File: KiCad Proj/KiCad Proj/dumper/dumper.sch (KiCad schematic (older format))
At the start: 2 parts, among them J2 SPI

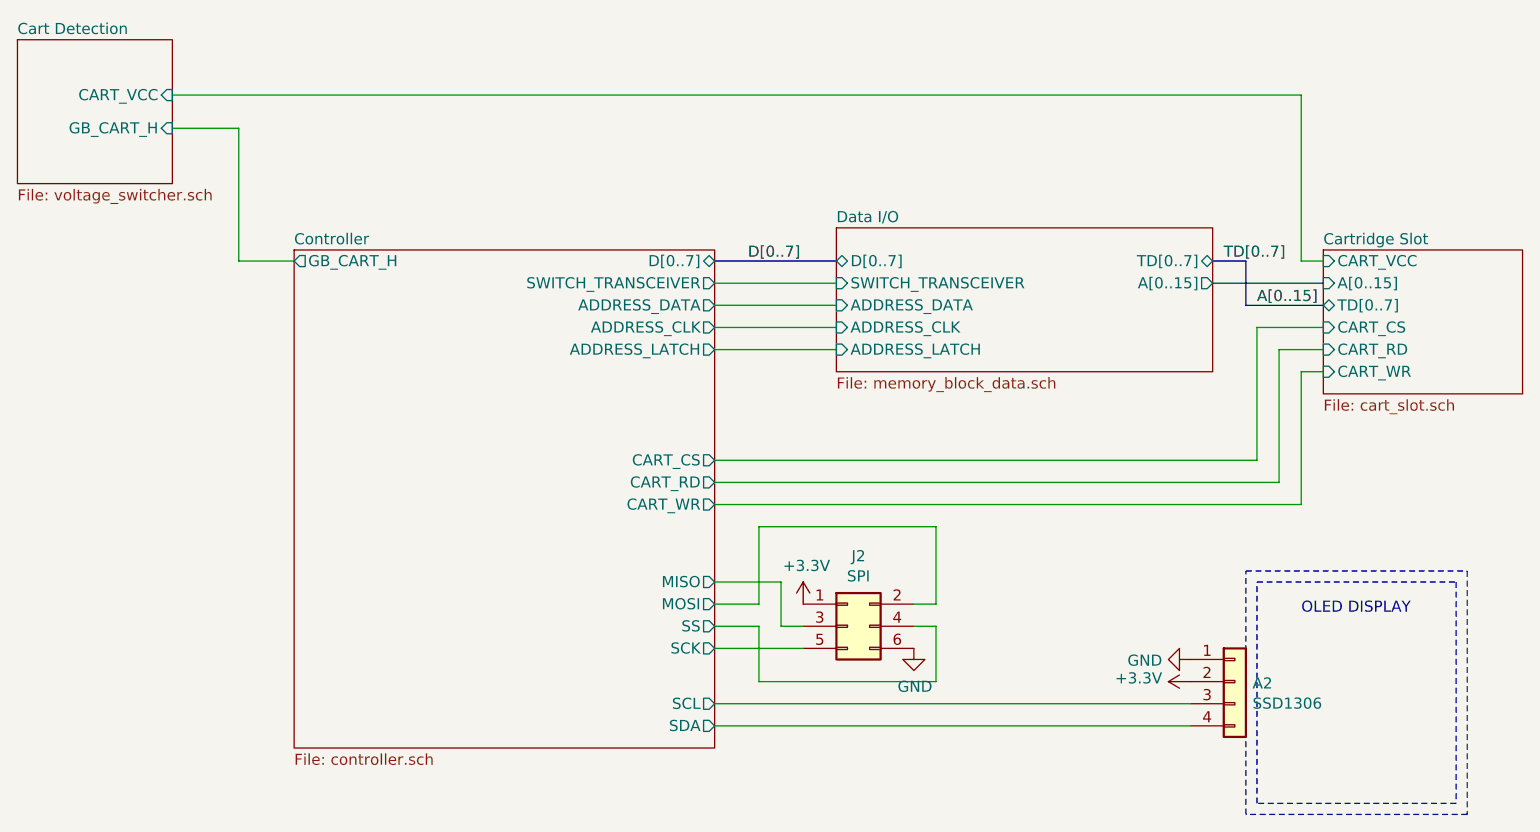
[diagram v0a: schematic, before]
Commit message: Fixed up the schematic and PCB for two very severe omissions
I forgot to translate the WR, RD, and CS pins and added a transceiver for those

I also forgot that the transceivers should have CART_VCC on VccB
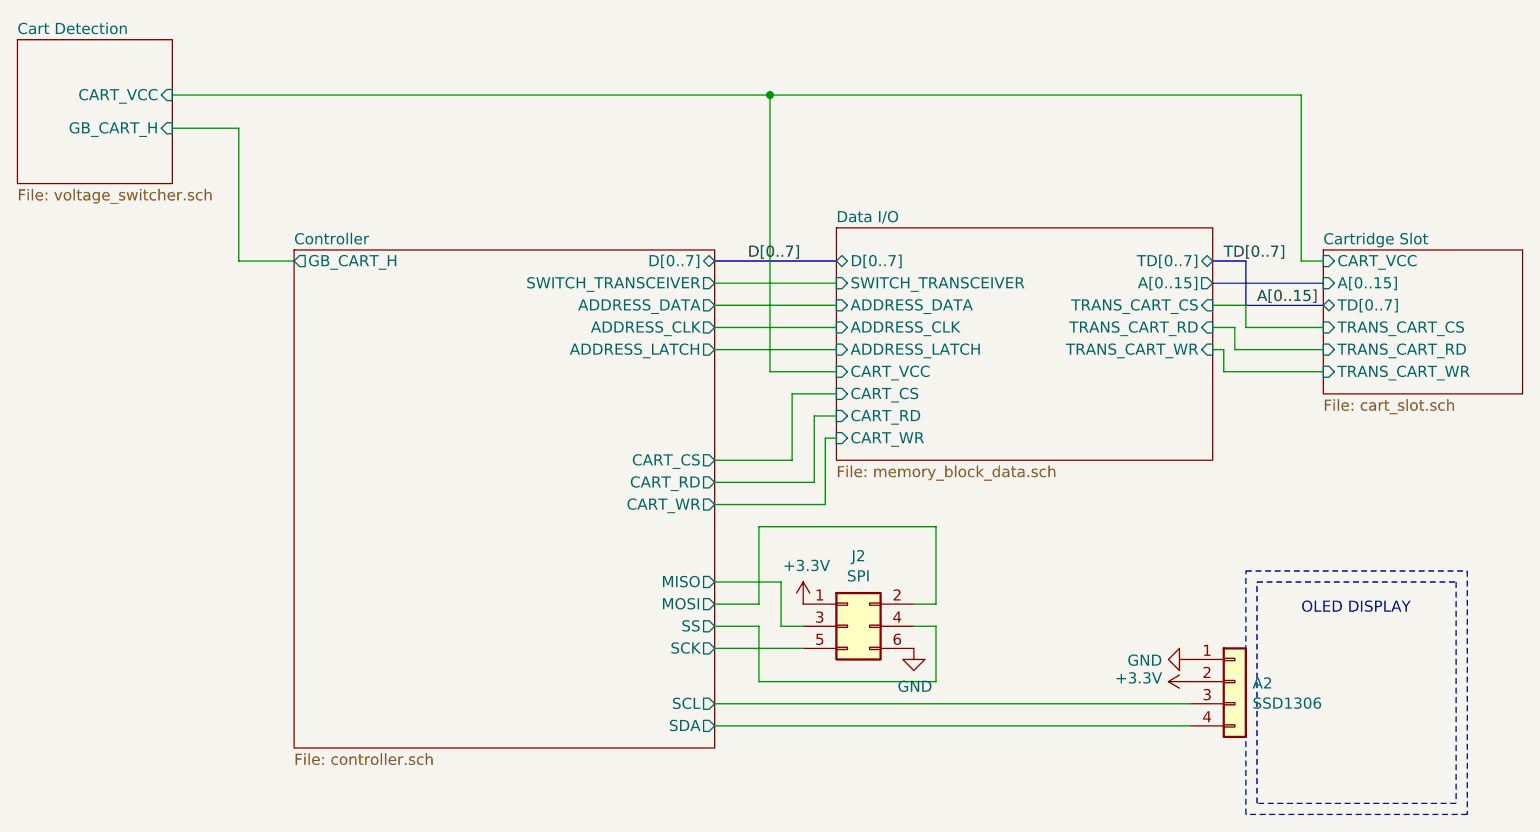
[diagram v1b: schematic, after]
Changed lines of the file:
@@
 	6300 3550 5750 3550
 Wire Wire Line
-	5750 4050 8200 4050
-Wire Wire Line
-	8200 4050 8200 3450
-Wire Wire Line
-	8200 3450 8500 3450
-Wire Wire Line
-	5750 4150 8300 4150
-Wire Wire Line
-	8300 4150 8300 3550
-Wire Wire Line
-	8300 3550 8500 3550
-Wire Wire Line
-	8500 3650 8400 3650
-Wire Wire Line
-	8400 3650 8400 4250
-Wire Wire Line
-	8400 4250 5750 4250
-Wire Wire Line
 	8400 2400 8400 3150
 Wire Wire Line
 	8400 3150 8500 3150
 Wire Wire Line
-	3300 2400 8400 2400
+	3300 2400 6000 2400
 Wire Wire Line
 	3300 2550 3600 2550
@@
 F2 "A[0..15]" I L 8500 3250 50
 F3 "CART_VCC" I L 8500 3150 50
-F4 "CART_CS" I L 8500 3450 50
-F5 "CART_RD" I L 8500 3550 50
-F6 "CART_WR" I L 8500 3650 50
+F4 "TRANS_CART_CS" I L 8500 3450 50
+F5 "TRANS_CART_RD" I L 8500 3550 50
+F6 "TRANS_CART_WR" I L 8500 3650 50
 F7 "TD[0..7]" B L 8500 3350 50
-$EndSheet
-$Sheet
-S 6300 3000 1700 650
-U 61204525
-F0 "Data I/O" 50
-F1 "memory_block_data.sch" 50
-F2 "D[0..7]" B L 6300 3150 50
-F3 "TD[0..7]" B R 8000 3150 50
-F4 "ADDRESS_DATA" I L 6300 3350 50
-F5 "ADDRESS_CLK" I L 6300 3450 50
-F6 "ADDRESS_LATCH" I L 6300 3550 50
-F7 "A[0..15]" O R 8000 3250 50
-F8 "SWITCH_TRANSCEIVER" I L 6300 3250 50
 $EndSheet
 Wire Bus Line
@@
 F3 "GB_CART_H" I R 3300 2550 50
 $EndSheet
+Wire Wire Line
+	6000 2400 6000 3650
+Wire Wire Line
+	6000 3650 6300 3650
+Connection ~ 6000 2400
+Wire Wire Line
+	6000 2400 8400 2400
+$Sheet
+S 6300 3000 1700 1050
+U 61204525
+F0 "Data I/O" 50
+F1 "memory_block_data.sch" 50
+F2 "D[0..7]" B L 6300 3150 50
+F3 "TD[0..7]" B R 8000 3150 50
+F4 "ADDRESS_DATA" I L 6300 3350 50
+F5 "ADDRESS_CLK" I L 6300 3450 50
+F6 "ADDRESS_LATCH" I L 6300 3550 50
+F7 "A[0..15]" O R 8000 3250 50
+F8 "SWITCH_TRANSCEIVER" I L 6300 3250 50
+F9 "CART_VCC" I L 6300 3650 50
+F10 "CART_CS" I L 6300 3750 50
+F11 "CART_RD" I L 6300 3850 50
+F12 "CART_WR" I L 6300 3950 50
+F13 "TRANS_CART_CS" I R 8000 3350 50
+F14 "TRANS_CART_RD" I R 8000 3450 50
+F15 "TRANS_CART_WR" I R 8000 3550 50
+$EndSheet
+Wire Wire Line
+	5750 4050 6100 4050
+Wire Wire Line
+	6100 4050 6100 3750
+Wire Wire Line
+	6100 3750 6300 3750
+Wire Wire Line
+	5750 4150 6200 4150
+Wire Wire Line
+	6200 4150 6200 3850
+Wire Wire Line
+	6200 3850 6300 3850
+Wire Wire Line
+	5750 4250 6250 4250
+Wire Wire Line
+	6250 4250 6250 3950
+Wire Wire Line
+	6250 3950 6300 3950
+Wire Wire Line
+	8000 3350 8150 3350
+Wire Wire Line
+	8150 3350 8150 3450
+Wire Wire Line
+	8150 3450 8500 3450
+Wire Wire Line
+	8000 3450 8100 3450
+Wire Wire Line
+	8100 3450 8100 3550
+Wire Wire Line
+	8100 3550 8500 3550
+Wire Wire Line
+	8000 3550 8050 3550
+Wire Wire Line
+	8050 3550 8050 3650
+Wire Wire Line
+	8050 3650 8500 3650
 $EndSCHEMATC
